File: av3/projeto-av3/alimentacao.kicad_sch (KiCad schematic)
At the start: 5 parts, among them J18 Jack-DC, U11 L7805

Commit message: Esquemático finalizado, faltando somente o PCB.
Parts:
- removed J18: Jack-DC, symbol Connector:Jack-DC
- added J10: Jack-DC, Connector_BarrelJack:BarrelJack_Horizontal, symbol Connector:Jack-DC
- C10: value C_Polarized -> 10uF/35V; footprint (none) -> Capacitor_SMD:CP_Elec_5x5.7
- C11, C12: value C -> 100nF; footprint (none) -> Capacitor_SMD:C_1206_3216Metric
- U11: footprint (none) -> Package_TO_SOT_THT:TO-220-3_Horizontal_TabDown
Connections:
- net GND: now also J10.2
- net at C10.1, C11.1, U11.1 (IN): now also J10.1

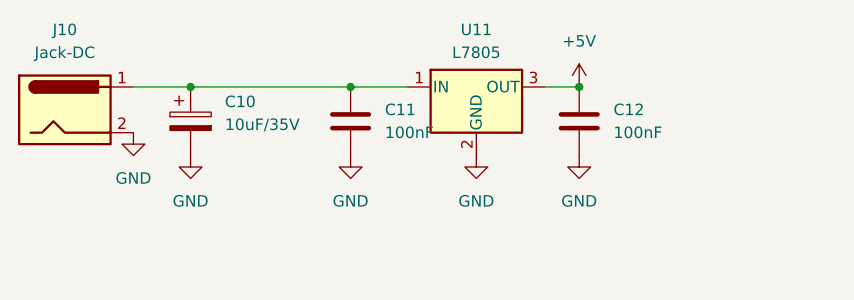
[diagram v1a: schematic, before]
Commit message: Referencias de componentes resetados; Progresso de 20% no PCB;
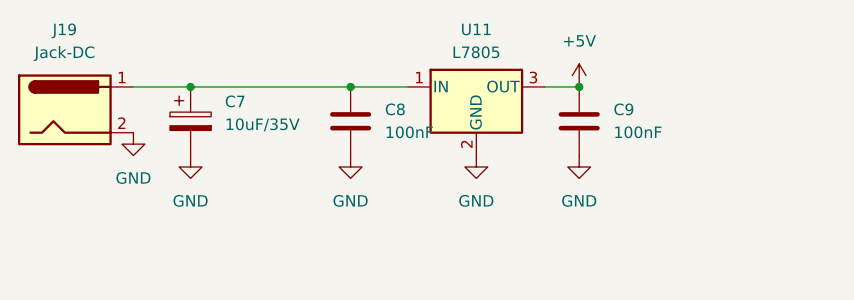
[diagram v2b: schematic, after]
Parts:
- renumbered C10 to C7, C11 to C8, C12 to C9, J10 to J19
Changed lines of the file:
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@@
 		(dnp no)
 		(fields_autoplaced yes)
-		(property "Reference" "C12"
+		(property "Reference" "C9"
 			(at 88.9 30.4799 0)
 			(effects
@@
 			(project "av3"
 				(path "/82998b71-606c-4e03-99b7-477e2a65cb94/5a7eb36d-627f-4d47-8a62-caf8a689718a"
-					(reference "C12")
+					(reference "C9")
 					(unit 1)
 				)
@@
 		(dnp no)
 		(fields_autoplaced yes)
-		(property "Reference" "#PWR057"
+		(property "Reference" "#PWR070"
 			(at 41.91 41.91 0)
 			(effects
@@
 			(project "av3"
 				(path "/82998b71-606c-4e03-99b7-477e2a65cb94/5a7eb36d-627f-4d47-8a62-caf8a689718a"
-					(reference "#PWR057")
+					(reference "#PWR070")
 					(unit 1)
 				)
@@
 		(dnp no)
 		(fields_autoplaced yes)
-		(property "Reference" "J10"
+		(property "Reference" "J19"
 			(at 27.94 21.59 0)
 			(effects
@@
 			(project "av3"
 				(path "/82998b71-606c-4e03-99b7-477e2a65cb94/5a7eb36d-627f-4d47-8a62-caf8a689718a"
-					(reference "J10")
+					(reference "J19")
 					(unit 1)
 				)
@@
 		(dnp no)
 		(fields_autoplaced yes)
-		(property "Reference" "#PWR056"
+		(property "Reference" "#PWR069"
 			(at 35.56 39.37 0)
 			(effects
@@
 			(project "av3"
 				(path "/82998b71-606c-4e03-99b7-477e2a65cb94/5a7eb36d-627f-4d47-8a62-caf8a689718a"
-					(reference "#PWR056")
+					(reference "#PWR069")
 					(unit 1)
 				)
@@
 		(dnp no)
 		(fields_autoplaced yes)
-		(property "Reference" "C10"
+		(property "Reference" "C7"
 			(at 45.72 29.5909 0)
 			(effects
@@
 			(project "av3"
 				(path "/82998b71-606c-4e03-99b7-477e2a65cb94/5a7eb36d-627f-4d47-8a62-caf8a689718a"
-					(reference "C10")
+					(reference "C7")
 					(unit 1)
 				)
@@
 		(dnp no)
 		(fields_autoplaced yes)
-		(property "Reference" "#PWR061"
+		(property "Reference" "#PWR073"
 			(at 85.09 41.91 0)
 			(effects
@@
 			(project "av3"
 				(path "/82998b71-606c-4e03-99b7-477e2a65cb94/5a7eb36d-627f-4d47-8a62-caf8a689718a"
-					(reference "#PWR061")
+					(reference "#PWR073")
 					(unit 1)
 				)
@@
 		(dnp no)
 		(fields_autoplaced yes)
-		(property "Reference" "#PWR060"
+		(property "Reference" "#PWR068"
 			(at 85.09 31.75 0)
 			(effects
@@
 			(project "av3"
 				(path "/82998b71-606c-4e03-99b7-477e2a65cb94/5a7eb36d-627f-4d47-8a62-caf8a689718a"
-					(reference "#PWR060")
+					(reference "#PWR068")
 					(unit 1)
 				)
@@
 		(dnp no)
 		(fields_autoplaced yes)
-		(property "Reference" "#PWR058"
+		(property "Reference" "#PWR071"
 			(at 59.69 41.91 0)
 			(effects
@@
 			(project "av3"
 				(path "/82998b71-606c-4e03-99b7-477e2a65cb94/5a7eb36d-627f-4d47-8a62-caf8a689718a"
-					(reference "#PWR058")
+					(reference "#PWR071")
 					(unit 1)
 				)
@@
 		(dnp no)
 		(fields_autoplaced yes)
-		(property "Reference" "C11"
+		(property "Reference" "C8"
 			(at 63.5 30.4799 0)
 			(effects
@@
 			(project "av3"
 				(path "/82998b71-606c-4e03-99b7-477e2a65cb94/5a7eb36d-627f-4d47-8a62-caf8a689718a"
-					(reference "C11")
+					(reference "C8")
 					(unit 1)
 				)
@@
 		(dnp no)
 		(fields_autoplaced yes)
-		(property "Reference" "#PWR059"
+		(property "Reference" "#PWR072"
 			(at 73.66 41.91 0)
 			(effects
@@
 			(project "av3"
 				(path "/82998b71-606c-4e03-99b7-477e2a65cb94/5a7eb36d-627f-4d47-8a62-caf8a689718a"
-					(reference "#PWR059")
-					(unit 1)
-				)
+					(reference "#PWR072")
+					(unit 1)
+				)
